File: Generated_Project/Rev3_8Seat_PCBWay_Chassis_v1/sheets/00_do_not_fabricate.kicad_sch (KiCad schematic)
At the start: 0 parts

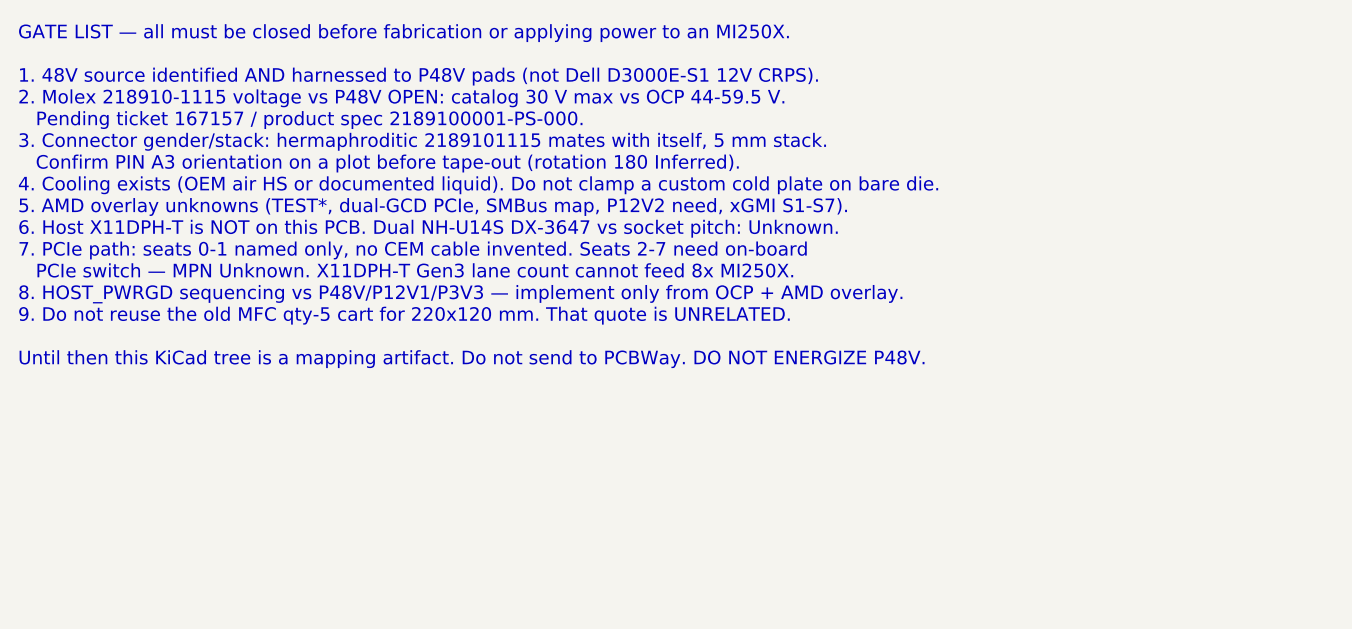
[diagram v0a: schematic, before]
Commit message: Raise Rev3 chassis to 8 electrically designed seats.
Name v1.0 power/PE/clock nets on all eight OAM seats toward two DNP
PM8536B-FEI (x8 per GCD), keep SB175 star + local P48V pours, and generate
the 12-layer 2.0 mm stuffed-switch target. First stuffing may still populate
two modules; the PCB does not need a respin for the other six.

Do not fabricate. Do not energize P48V.

Co-authored-by: zivzancoeli-commits <zivzancoeli-commits@users.noreply.github.com>
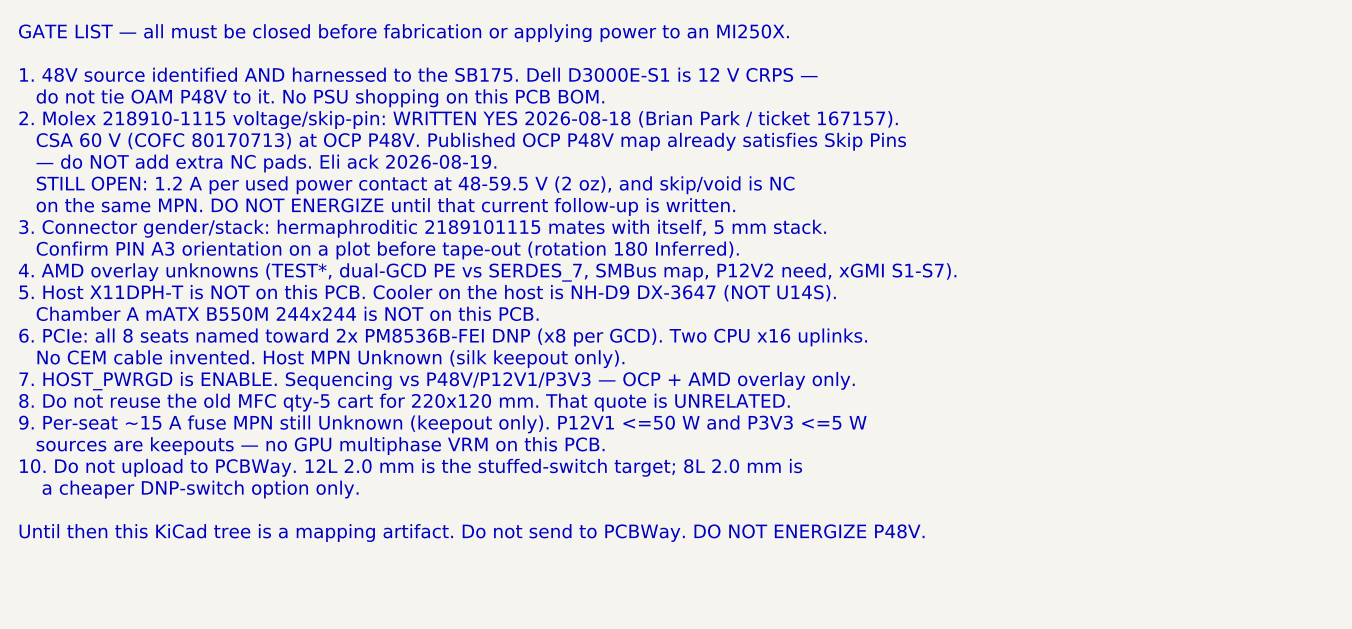
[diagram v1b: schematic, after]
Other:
- note added: "GATE LIST — all must be closed before fabrication or applying power to an MI250X. 1. 48V source identified AND harnessed to the SB175. Dell D3000E-S1 is 12 V CRPS — do not tie OAM P48V to it. No PSU shopping on this PCB BOM. 2. Molex 218910-1115 voltage/skip-pin: WRITTEN YES 2026-08-18 (Brian Park / ticket 167157). CSA 60 V (COFC 80170713) at OCP P48V. Published OCP P48V map already satisfies Ski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"
- note removed: "GATE LIST — all must be closed before fabrication or applying power to an MI250X. 1. 48V source identified AND harnessed to P48V pads (not Dell D3000E-S1 12V CRPS). 2. Molex 218910-1115 voltage vs P48V OPEN: catalog 30 V max vs OCP 44-59.5 V. Pending ticket 167157 / product spec 2189100001-PS-000. 3. Connector gender/stack: hermaphroditic 2189101115 mates with itself, 5 mm stack. Confirm PIN A3 o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"
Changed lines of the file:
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@@
 		(date "2026-08-21")
 		(rev "Rev3_8Seat_PCBWay_v1")
-		(comment 1 "DO NOT FABRICATE. DO NOT ENERGIZE P48V. Ticket 167157 open.")
-		(comment 2 "Documentation sheet — no invented nets")
-		(comment 3 "Pin names: OAM Pin map rev 1.0.xlsx — OCP generic, NOT AMD overlay")
-		(comment 4 "r2.0 maps UNUSABLE. P3V3=2 Conn0 C1/C2. 8-seat PCBWay chassis stub.")
+        (comment 1 "DO NOT FABRICATE. DO NOT ENERGIZE P48V. Molex 60V written 2026-08-18; 1.2A/contact OPEN.")
+        (comment 2 "Documentation sheet — no invented nets")
+        (comment 3 "Pin names: OAM Pin map rev 1.0.xlsx — OCP generic, NOT AMD overlay")
+        (comment 4 "r2.0 UNUSABLE. P3V3=Conn0 C1/C2. 12L 2.0mm stuffed-switch TARGET. Star-fed P48V.")
 	)
-	(text "GATE LIST — all must be closed before fabrication or applying power to an MI250X.\n\n1. 48V source identified AND harnessed to P48V pads (not Dell D3000E-S1 12V CRPS).\n2. Molex 218910-1115 voltage vs P48V OPEN: catalog 30 V max vs OCP 44-59.5 V.\n   Pending ticket 167157 / product spec 2189100001-PS-000.\n3. Connector gender/stack: hermaphroditic 2189101115 mates with itself, 5 mm stack.\n   Confirm PIN A3 orientation on a plot before tape-out (rotation 180 Inferred).\n4. Cooling exists (OEM air HS or documented liquid). Do not clamp a custom cold plate on bare die.\n5. AMD overlay unknowns (TEST*, dual-GCD PCIe, SMBus map, P12V2 need, xGMI S1-S7).\n6. Host X11DPH-T is NOT on this PCB. Dual NH-U14S DX-3647 vs socket pitch: Unknown.\n7. PCIe path: seats 0-1 named only, no CEM cable invented. Seats 2-7 need on-board\n   PCIe switch — MPN Unknown. X11DPH-T Gen3 lane count cannot feed 8x MI250X.\n8. HOST_PWRGD sequencing vs P48V/P12V1/P3V3 — implement only from OCP + AMD overlay.\n9. Do not reuse the old MFC qty-5 cart for 220x120 mm. That quote is UNRELATED.\n\nUntil then this KiCad tree is a mapping artifact. Do not send to PCBWay. DO NOT ENERGIZE P48V.\n"
+	(text "GATE LIST — all must be closed before fabrication or applying power to an MI250X.\n\n1. 48V source identified AND harnessed to the SB175. Dell D3000E-S1 is 12 V CRPS —\n   do not tie OAM P48V to it. No PSU shopping on this PCB BOM.\n2. Molex 218910-1115 voltage/skip-pin: WRITTEN YES 2026-08-18 (Brian Park / ticket 167157).\n   CSA 60 V (COFC 80170713) at OCP P48V. Published OCP P48V map already satisfies Skip Pins\n   — do NOT add extra NC pads. Eli ack 2026-08-19.\n   STILL OPEN: 1.2 A per used power contact at 48-59.5 V (2 oz), and skip/void is NC\n   on the same MPN. DO NOT ENERGIZE until that current follow-up is written.\n3. Connector gender/stack: hermaphroditic 2189101115 mates with itself, 5 mm stack.\n   Confirm PIN A3 orientation on a plot before tape-out (rotation 180 Inferred).\n4. AMD overlay unknowns (TEST*, dual-GCD PE vs SERDES_7, SMBus map, P12V2 need, xGMI S1-S7).\n5. Host X11DPH-T is NOT on this PCB. Cooler on the host is NH-D9 DX-3647 (NOT U14S).\n   Chamber A mATX B550M 244x244 is NOT on this PCB.\n6. PCIe: all 8 seats named toward 2x PM8536B-FEI DNP (x8 per GCD). Two CPU x16 uplinks.\n   No CEM cable invented. Host MPN Unknown (silk keepout only).\n7. HOST_PWRGD is ENABLE. Sequencing vs P48V/P12V1/P3V3 — OCP + AMD overlay only.\n8. Do not reuse the old MFC qty-5 cart for 220x120 mm. That quote is UNRELATED.\n9. Per-seat ~15 A fuse MPN still Unknown (keepout only). P12V1 <=50 W and P3V3 <=5 W\n   sources are keepouts — no GPU multiphase VRM on this PCB.\n10. Do not upload to PCBWay. 12L 2.0 mm is the stuffed-switch target; 8L 2.0 mm is\n    a cheaper DNP-switch option only.\n\nUntil then this KiCad tree is a mapping artifact. Do not send to PCBWay. DO NOT ENERGIZE P48V.\n"
 		(exclude_from_sim no)
 		(at 20.32 20.32 0)

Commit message: Label PEX8780-AB80BI G as the only switch CANDIDATE (DNP).
Keepout is one 35 mm 1156-FCBGA for 8x x8 Gen3 plus one x16 host uplink.
Do not invent a second MPN. Do not stuff. 8-layer is likely if this BGA
is ever assembled; PCBWay 1156-FCBGA attach remains Unknown.

Still do not fabricate or energize P48V. No xGMI, no CEM.

Co-authored-by: zivzancoeli-commits <zivzancoeli-commits@users.noreply.github.com>
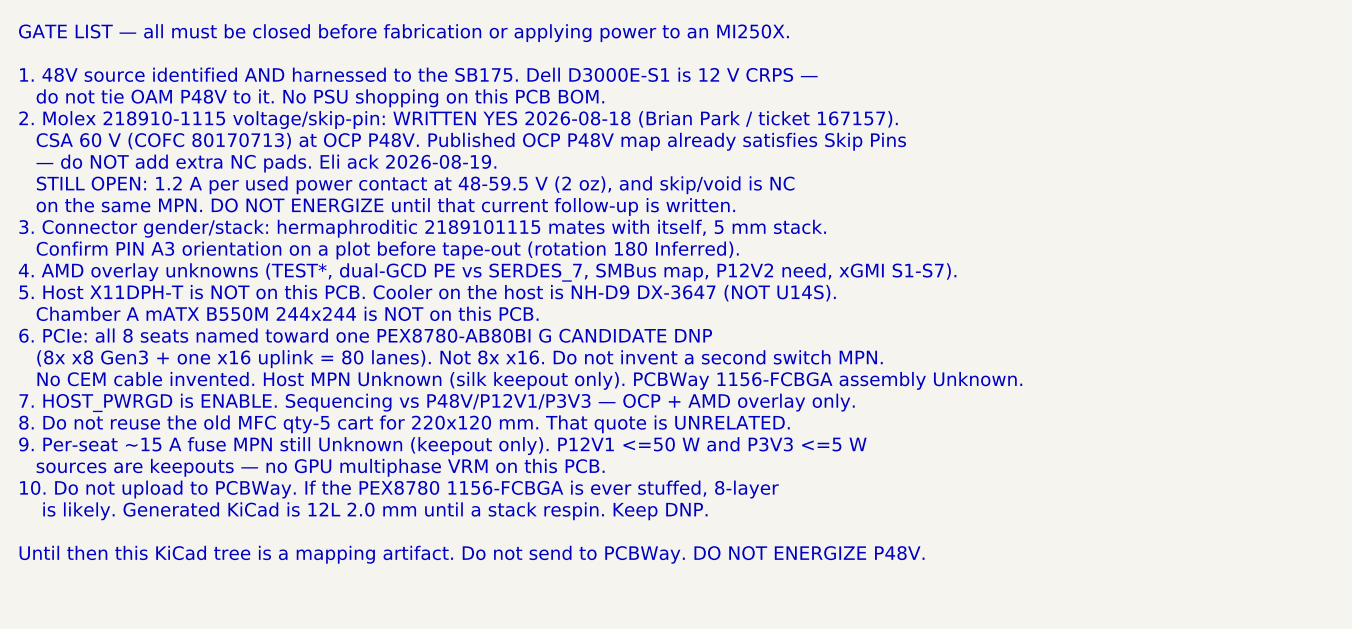
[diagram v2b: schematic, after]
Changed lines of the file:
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@@
         (comment 4 "r2.0 UNUSABLE. P3V3=Conn0 C1/C2. 12L 2.0mm stuffed-switch TARGET. Star-fed P48V.")
 	)
-	(text "GATE LIST — all must be closed before fabrication or applying power to an MI250X.\n\n1. 48V source identified AND harnessed to the SB175. Dell D3000E-S1 is 12 V CRPS —\n   do not tie OAM P48V to it. No PSU shopping on this PCB BOM.\n2. Molex 218910-1115 voltage/skip-pin: WRITTEN YES 2026-08-18 (Brian Park / ticket 167157).\n   CSA 60 V (COFC 80170713) at OCP P48V. Published OCP P48V map already satisfies Skip Pins\n   — do NOT add extra NC pads. Eli ack 2026-08-19.\n   STILL OPEN: 1.2 A per used power contact at 48-59.5 V (2 oz), and skip/void is NC\n   on the same MPN. DO NOT ENERGIZE until that current follow-up is written.\n3. Connector gender/stack: hermaphroditic 2189101115 mates with itself, 5 mm stack.\n   Confirm PIN A3 orientation on a plot before tape-out (rotation 180 Inferred).\n4. AMD overlay unknowns (TEST*, dual-GCD PE vs SERDES_7, SMBus map, P12V2 need, xGMI S1-S7).\n5. Host X11DPH-T is NOT on this PCB. Cooler on the host is NH-D9 DX-3647 (NOT U14S).\n   Chamber A mATX B550M 244x244 is NOT on this PCB.\n6. PCIe: all 8 seats named toward 2x PM8536B-FEI DNP (x8 per GCD). Two CPU x16 uplinks.\n   No CEM cable invented. Host MPN Unknown (silk keepout only).\n7. HOST_PWRGD is ENABLE. Sequencing vs P48V/P12V1/P3V3 — OCP + AMD overlay only.\n8. Do not reuse the old MFC qty-5 cart for 220x120 mm. That quote is UNRELATED.\n9. Per-seat ~15 A fuse MPN still Unknown (keepout only). P12V1 <=50 W and P3V3 <=5 W\n   sources are keepouts — no GPU multiphase VRM on this PCB.\n10. Do not upload to PCBWay. 12L 2.0 mm is the stuffed-switch target; 8L 2.0 mm is\n    a cheaper DNP-switch option only.\n\nUntil then this KiCad tree is a mapping artifact. Do not send to PCBWay. DO NOT ENERGIZE P48V.\n"
+	(text "GATE LIST — all must be closed before fabrication or applying power to an MI250X.\n\n1. 48V source identified AND harnessed to the SB175. Dell D3000E-S1 is 12 V CRPS —\n   do not tie OAM P48V to it. No PSU shopping on this PCB BOM.\n2. Molex 218910-1115 voltage/skip-pin: WRITTEN YES 2026-08-18 (Brian Park / ticket 167157).\n   CSA 60 V (COFC 80170713) at OCP P48V. Published OCP P48V map already satisfies Skip Pins\n   — do NOT add extra NC pads. Eli ack 2026-08-19.\n   STILL OPEN: 1.2 A per used power contact at 48-59.5 V (2 oz), and skip/void is NC\n   on the same MPN. DO NOT ENERGIZE until that current follow-up is written.\n3. Connector gender/stack: hermaphroditic 2189101115 mates with itself, 5 mm stack.\n   Confirm PIN A3 orientation on a plot before tape-out (rotation 180 Inferred).\n4. AMD overlay unknowns (TEST*, dual-GCD PE vs SERDES_7, SMBus map, P12V2 need, xGMI S1-S7).\n5. Host X11DPH-T is NOT on this PCB. Cooler on the host is NH-D9 DX-3647 (NOT U14S).\n   Chamber A mATX B550M 244x244 is NOT on this PCB.\n6. PCIe: all 8 seats named toward one PEX8780-AB80BI G CANDIDATE DNP\n   (8x x8 Gen3 + one x16 uplink = 80 lanes). Not 8x x16. Do not invent a second switch MPN.\n   No CEM cable invented. Host MPN Unknown (silk keepout only). PCBWay 1156-FCBGA assembly Unknown.\n7. HOST_PWRGD is ENABLE. Sequencing vs P48V/P12V1/P3V3 — OCP + AMD overlay only.\n8. Do not reuse the old MFC qty-5 cart for 220x120 mm. That quote is UNRELATED.\n9. Per-seat ~15 A fuse MPN still Unknown (keepout only). P12V1 <=50 W and P3V3 <=5 W\n   sources are keepouts — no GPU multiphase VRM on this PCB.\n10. Do not upload to PCBWay. If the PEX8780 1156-FCBGA is ever stuffed, 8-layer\n    is likely. Generated KiCad is 12L 2.0 mm until a stack respin. Keep DNP.\n\nUntil then this KiCad tree is a mapping artifact. Do not send to PCBWay. DO NOT ENERGIZE P48V.\n"
 		(exclude_from_sim no)
 		(at 20.32 20.32 0)

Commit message: Make PM8536B-FEI the PRIMARY switch keepout (DNP x2).
Two 37.5 mm 1311-FCBGA courtyards, x8 per GCD (SW0 seats 0-3, SW1 4-7),
two CPU x16 uplinks. PEX8780 stays a cheaper 80-lane alt in docs only.
GCD1 = SERDES_7 remains Inferred. No CEM, no xGMI, do not fabricate.

Co-authored-by: zivzancoeli-commits <zivzancoeli-commits@users.noreply.github.com>
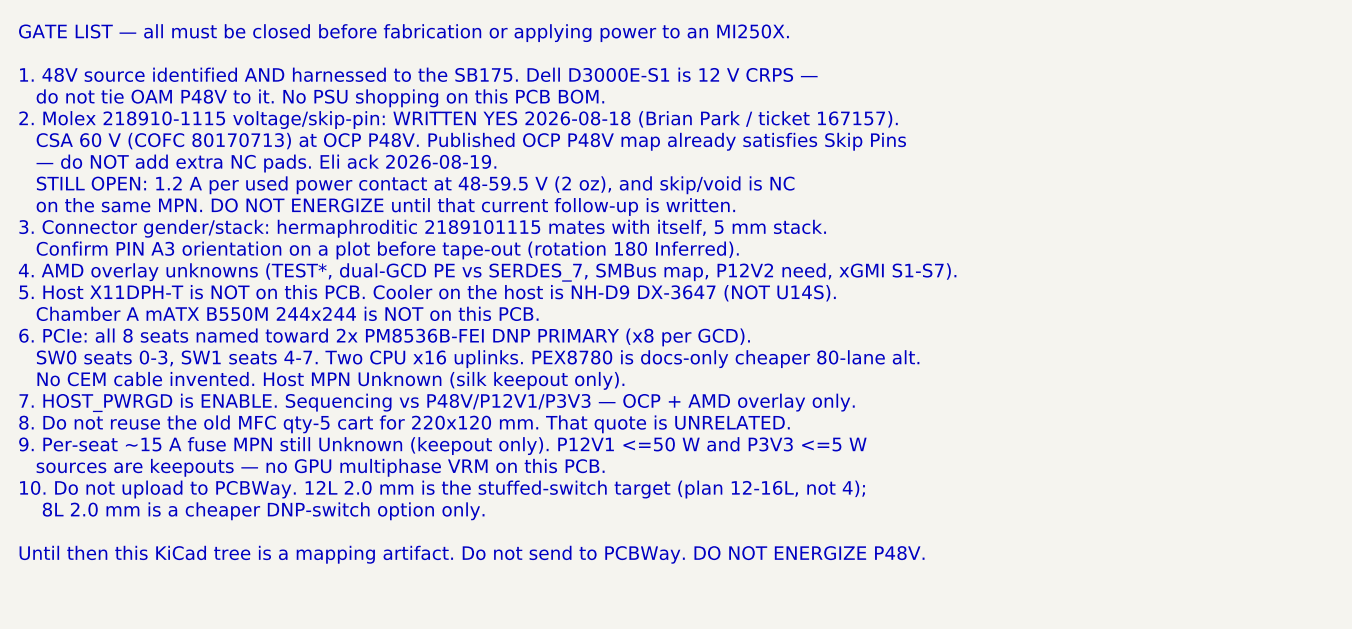
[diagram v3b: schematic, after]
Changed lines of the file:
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@@
         (comment 2 "Documentation sheet — no invented nets")
         (comment 3 "Pin names: OAM Pin map rev 1.0.xlsx — OCP generic, NOT AMD overlay")
-        (comment 4 "r2.0 UNUSABLE. P3V3=Conn0 C1/C2. 12L 2.0mm stuffed-switch TARGET. Star-fed P48V.")
+        (comment 4 "r2.0 UNUSABLE. P3V3=Conn0 C1/C2. 12L 2.0mm stuffed-switch TARGET. 2x PM8536 DNP. Star-fed P48V.")
 	)
-	(text "GATE LIST — all must be closed before fabrication or applying power to an MI250X.\n\n1. 48V source identified AND harnessed to the SB175. Dell D3000E-S1 is 12 V CRPS —\n   do not tie OAM P48V to it. No PSU shopping on this PCB BOM.\n2. Molex 218910-1115 voltage/skip-pin: WRITTEN YES 2026-08-18 (Brian Park / ticket 167157).\n   CSA 60 V (COFC 80170713) at OCP P48V. Published OCP P48V map already satisfies Skip Pins\n   — do NOT add extra NC pads. Eli ack 2026-08-19.\n   STILL OPEN: 1.2 A per used power contact at 48-59.5 V (2 oz), and skip/void is NC\n   on the same MPN. DO NOT ENERGIZE until that current follow-up is written.\n3. Connector gender/stack: hermaphroditic 2189101115 mates with itself, 5 mm stack.\n   Confirm PIN A3 orientation on a plot before tape-out (rotation 180 Inferred).\n4. AMD overlay unknowns (TEST*, dual-GCD PE vs SERDES_7, SMBus map, P12V2 need, xGMI S1-S7).\n5. Host X11DPH-T is NOT on this PCB. Cooler on the host is NH-D9 DX-3647 (NOT U14S).\n   Chamber A mATX B550M 244x244 is NOT on this PCB.\n6. PCIe: all 8 seats named toward one PEX8780-AB80BI G CANDIDATE DNP\n   (8x x8 Gen3 + one x16 uplink = 80 lanes). Not 8x x16. Do not invent a second switch MPN.\n   No CEM cable invented. Host MPN Unknown (silk keepout only). PCBWay 1156-FCBGA assembly Unknown.\n7. HOST_PWRGD is ENABLE. Sequencing vs P48V/P12V1/P3V3 — OCP + AMD overlay only.\n8. Do not reuse the old MFC qty-5 cart for 220x120 mm. That quote is UNRELATED.\n9. Per-seat ~15 A fuse MPN still Unknown (keepout only). P12V1 <=50 W and P3V3 <=5 W\n   sources are keepouts — no GPU multiphase VRM on this PCB.\n10. Do not upload to PCBWay. If the PEX8780 1156-FCBGA is ever stuffed, 8-layer\n    is likely. Generated KiCad is 12L 2.0 mm until a stack respin. Keep DNP.\n\nUntil then this KiCad tree is a mapping artifact. Do not send to PCBWay. DO NOT ENERGIZE P48V.\n"
+	(text "GATE LIST — all must be closed before fabrication or applying power to an MI250X.\n\n1. 48V source identified AND harnessed to the SB175. Dell D3000E-S1 is 12 V CRPS —\n   do not tie OAM P48V to it. No PSU shopping on this PCB BOM.\n2. Molex 218910-1115 voltage/skip-pin: WRITTEN YES 2026-08-18 (Brian Park / ticket 167157).\n   CSA 60 V (COFC 80170713) at OCP P48V. Published OCP P48V map already satisfies Skip Pins\n   — do NOT add extra NC pads. Eli ack 2026-08-19.\n   STILL OPEN: 1.2 A per used power contact at 48-59.5 V (2 oz), and skip/void is NC\n   on the same MPN. DO NOT ENERGIZE until that current follow-up is written.\n3. Connector gender/stack: hermaphroditic 2189101115 mates with itself, 5 mm stack.\n   Confirm PIN A3 orientation on a plot before tape-out (rotation 180 Inferred).\n4. AMD overlay unknowns (TEST*, dual-GCD PE vs SERDES_7, SMBus map, P12V2 need, xGMI S1-S7).\n5. Host X11DPH-T is NOT on this PCB. Cooler on the host is NH-D9 DX-3647 (NOT U14S).\n   Chamber A mATX B550M 244x244 is NOT on this PCB.\n6. PCIe: all 8 seats named toward 2x PM8536B-FEI DNP PRIMARY (x8 per GCD).\n   SW0 seats 0-3, SW1 seats 4-7. Two CPU x16 uplinks. PEX8780 is docs-only cheaper 80-lane alt.\n   No CEM cable invented. Host MPN Unknown (silk keepout only).\n7. HOST_PWRGD is ENABLE. Sequencing vs P48V/P12V1/P3V3 — OCP + AMD overlay only.\n8. Do not reuse the old MFC qty-5 cart for 220x120 mm. That quote is UNRELATED.\n9. Per-seat ~15 A fuse MPN still Unknown (keepout only). P12V1 <=50 W and P3V3 <=5 W\n   sources are keepouts — no GPU multiphase VRM on this PCB.\n10. Do not upload to PCBWay. 12L 2.0 mm is the stuffed-switch target (plan 12-16L, not 4);\n    8L 2.0 mm is a cheaper DNP-switch option only.\n\nUntil then this KiCad tree is a mapping artifact. Do not send to PCBWay. DO NOT ENERGIZE P48V.\n"
 		(exclude_from_sim no)
 		(at 20.32 20.32 0)
